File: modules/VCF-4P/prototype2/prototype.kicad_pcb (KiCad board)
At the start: 6 copper layers, 40.6 x 130.8 mm, 37 parts, among them J1 Conn_01x09, U1 TL074, U2 SSI2140

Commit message: VCF-4P: prototype2 - get cutoff CV from bus
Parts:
- removed RV1: 100K, -lmp-misc:Potentiometer_Bourns_3310R_Top
- moved R1 43.2 mm to (99.1, 50.8)
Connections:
- R1 pad 1: Net-(R1-Pad1) -> BUS-CV
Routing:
- net Net-(R1-Pad2): track 38.8 -> 74.4 mm, vias 2 -> 4
- net Net-(R1-Pad1): track 26.2 -> 0.00 mm, vias 2 -> 0
- net (no net): track 284.5 -> 304.8 mm
- net BUS-CV: track 0.00 -> 17.8 mm, vias 0 -> 1
- net GND: track 318.0 -> 305.3 mm, vias 11 -> 9
- net +12V: track 202.8 -> 192.1 mm, vias 7 -> 5

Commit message: VCF-4P: prototype2 - wip
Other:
- board text added: "BUS"
- board text removed: "+5V"
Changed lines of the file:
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@@
     )
   )
-  (gr_circle (center 114.449903 55.245) (end 115.869806 55.245) (layer "Dwgs.User") (width 0.254) (fill none))
-  (gr_circle (center 97.304903 97.155) (end 98.724806 97.155) (layer "Dwgs.User") (width 0.254) (fill none))
-  (gr_circle (center 102.384903 50.165) (end 103.804806 50.165) (layer "Dwgs.User") (width 0.254) (fill none))
   (gr_line (start 123.19 168.91) (end 82.55 168.91) (layer "Edge.Cuts") (width 0.1))
   (gr_line (start 123.19 38.1) (end 123.19 168.91) (layer "Edge.Cuts") (width 0.1))
@@
     (effects (font (size 1.524 1.524) (thickness 0.254)))
   )
-  (gr_text "+5V" (at 97.155 46.355) (layer "Cmts.User")
+  (gr_text "BUS" (at 95.25 40.005) (layer "Cmts.User")
     (effects (font (size 1.524 1.524) (thickness 0.254)))
   )

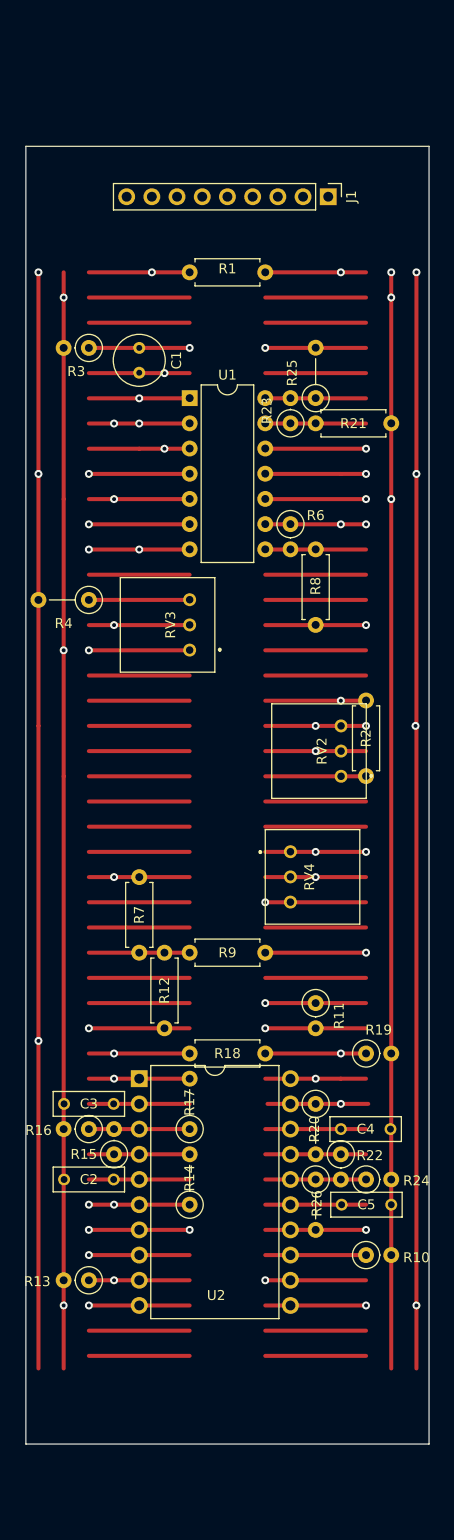
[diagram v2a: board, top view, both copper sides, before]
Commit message: VCF-4P: prototype2 - add input level control
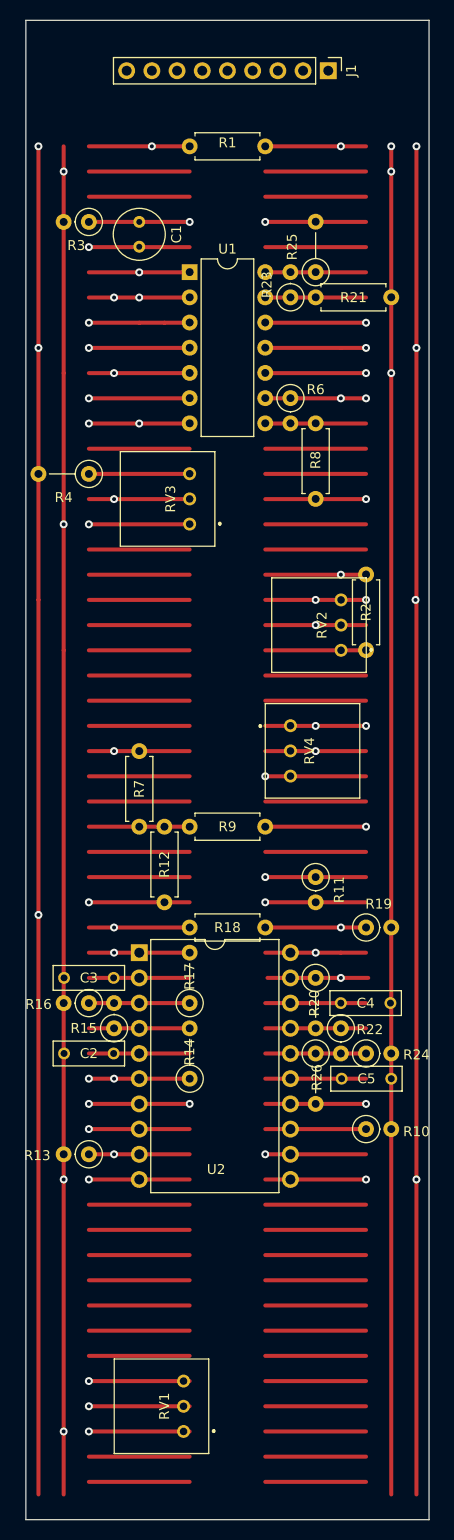
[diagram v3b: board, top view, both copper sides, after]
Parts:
- added RV1: 100K, -lmp-misc:Potentiometer_Bourns_3310R_Top, F.Cu at (96.5, 165.1)
- R2: value 153K -> 160K
- R3: value 1M -> 100K
- R8: value 53K -> 47K
- RV4: value 5K -> 10K
- moved C2 12.7 mm to (91.4, 129.5)
- moved R10 12.7 mm to (116.8, 137.2)
- moved R13 12.7 mm to (88.9, 139.7)
- moved R24 12.7 mm to (116.8, 129.5)
- moved R26 12.7 mm to (111.8, 129.5)
- moved U2 12.7 mm to (94.0, 119.4)
- moved R6 12.7 mm to (109.2, 63.5)
- moved C1 12.7 mm to (94.0, 45.7)
- moved C3 12.7 mm to (91.4, 121.9)
- moved C4 12.7 mm to (114.3, 124.5)
- moved R16 12.7 mm to (88.9, 124.5)
- moved R17 12.7 mm to (99.1, 124.5)
- moved R2 12.7 mm to (116.8, 88.9)
- moved R20 12.7 mm to (111.8, 121.9)
- moved R3 12.7 mm to (88.9, 45.7)
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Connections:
- U1 pad 3: Net-(C1-Pad2) -> Net-(U1-Pad3)
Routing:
- net (no net): track 304.8 -> 477.5 mm
- net Net-(U1-Pad3): track 0.00 -> 134.6 mm, vias 0 -> 2
- net Net-(C1-Pad2): track 27.9 -> 139.3 mm
- net GND: track 305.3 -> 368.8 mm, vias 9 -> 11
- net -12V: track 181.4 -> 206.8 mm
- net +12V: track 192.1 -> 217.5 mm
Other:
- board size 40.6 x 130.8 mm -> 40.6 x 151.1 mm
- board text added: "50"
